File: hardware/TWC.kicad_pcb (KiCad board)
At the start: 2 copper layers, 40 x 75 mm, 46 parts, among them J1 Screw_Terminal_01x04, J2 Conn_02x05_Odd_Even, J3 Conn_02x05_Odd_Even, J4 Conn_01x10_Male, J6 Screw_Terminal_01x02, SW1 SW_Push, SW2 SW_Push, U1 MAX3485, U2 Si7021-A20, U3 TPS56339DDC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

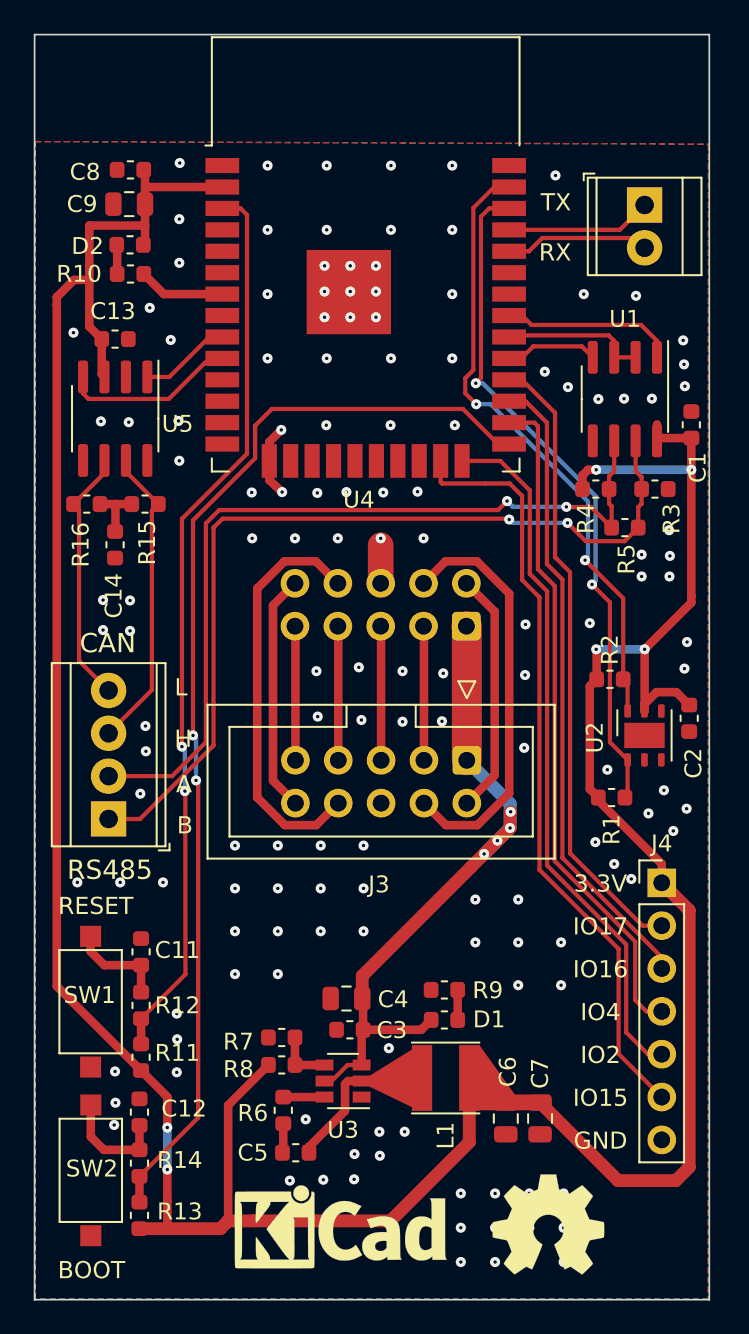
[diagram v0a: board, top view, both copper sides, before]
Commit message: Many small updates, including changing the Buck Converter and temperature sensor to more available parts, changed the screw terminals to the final footprint (0.1" pitch)
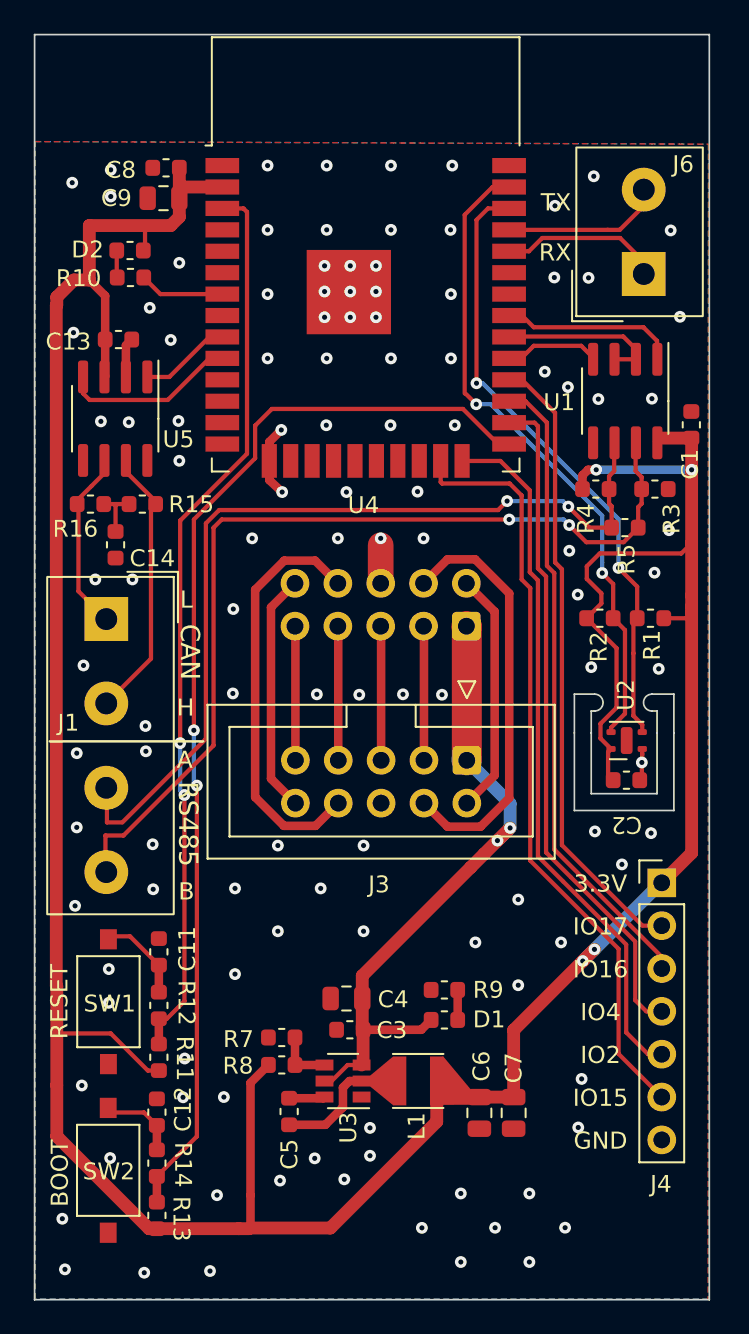
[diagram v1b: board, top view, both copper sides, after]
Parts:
- removed R6: 30, Capacitor_SMD:C_0603_1608Metric
- removed REF**: KiCad-Logo_5mm_SilkScreen, Symbol:KiCad-Logo_5mm_SilkScreen
- removed REF**: OSHW-Symbol_6.7x6mm_SilkScreen, Symbol:OSHW-Symbol_6.7x6mm_SilkScreen
- J1: footprint TerminalBlock_TE-Connectivity:TerminalBlock_TE_282834-4_1x04_P2.54mm_Horizontal -> TerminalBlock_Altech:Altech_AK500_1x04_P5.00
- J6: footprint TerminalBlock_TE-Connectivity:TerminalBlock_TE_282834-2_1x02_P2.54mm_Horizontal -> TerminalBlock_Altech:Altech_AK500_1x02_P5.00
- L1: value 4.7uH -> 3.3uH; footprint Inductor_SMD:L_Taiyo-Yuden_NR-40xx -> Inductor_SMD:L_Taiyo-Yuden_NR-30xx
- R1, R10, R11, R12, R13, R14, R2, R7, R9: footprint Capacitor_SMD:C_0603_1608Metric -> Resistor_SMD:R_0603_1608Metric
- R8: value 31.6 -> 33.2k; footprint Capacitor_SMD:C_0603_1608Metric -> Resistor_SMD:R_0603_1608Metric
- SW1, SW2: footprint Button_Switch_SMD:SW_SPST_CK_PTS636_SX25_XMTR_LFS -> Button_Switch_SMD:SW_SPST_TS_1101_X_X
- U1: value MAX3485 -> SN65HVD11DR
- U2: value Si7021-A20 -> SHTC3; footprint Package_DFN_QFN:DFN-6-1EP_3x3mm_P1mm_EP1.5x2.4mm -> Sensor_Humidity:Sensirion_DFN-4-1EP_2x2mm_P1mm_EP0.7x1.6mm
- U3: value TPS56339DDC -> TPS562201DDCR
- moved J1 11.9 mm to (64.2, 59.6), turned to -90 degrees
- moved R1 10.7 mm to (93.5, 59.6)
- moved C2 5.22 mm to (95.1, 69.2), turned to 0 degrees
- moved R2 4.35 mm to (96.5, 59.6), turned to 180 degrees
- moved J6 4.09 mm to (96.1, 39.2), turned to 90 degrees
- moved C5 2.48 mm to (75.1, 88.8), turned to -90 degrees
- moved C8 2.11 mm to (67.8, 32.9)
- moved C9 2.06 mm to (67.6, 34.7)
- moved L1 1.64 mm to (82.7, 87.0)
- moved C6 1.60 mm to (86.4, 88.9)
- moved C7 1.60 mm to (88.4, 88.9)
- moved U2 1.10 mm to (95.1, 66.8), turned to 180 degrees
- moved SW1 1.05 mm to (64.4, 82.3)
- moved C11 1.05 mm to (67.4, 79.4)
- moved R11 1.05 mm to (67.4, 85.6)
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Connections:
- C5 pad 1: Net-(C5-Pad1) -> /VBST
- J1 pad 1: /B -> /CANL
- J1 pad 2: /A -> /CANH
- J1 pad 3: /CANH -> /A
- J1 pad 4: /CANL -> /B
- J6 pad 1: /TX -> /RX
- J6 pad 2: /RX -> /TX
- U2 pad 1: /SDA -> GND
- U2 pad 2: GND -> /SCL
- U2 pad 3: Net-(U2-Pad3) -> /SDA
- U2 pad 4: Net-(U2-Pad4) -> +3V3
- U2 pad 5: +3V3 -> Net-(U2-Pad5)
- U3 pad 6: Net-(R6-Pad1) -> /VBST
- U4 pad 36: /SDA -> /SCL
- U4 pad 37: /SCL -> /SDA
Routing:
- net GND: track 6.57 -> 11.1 mm, vias 144 -> 118
- net /A: track 50.2 -> 54.5 mm
- net /B: track 52.6 -> 55.4 mm
- net Net-(R6-Pad1): track 2.44 -> 0.00 mm
- net /CANL: track 15.3 -> 12.9 mm
- net /VBST: track 0.00 -> 2.13 mm
- net /SDA: track 40.6 -> 38.7 mm
- net VCC: track 40.8 -> 39.0 mm, vias 4 -> 2
- net /CANH: track 18.2 -> 16.4 mm
- net Net-(C5-Pad1): track 1.75 -> 0.00 mm
- net +3V3: track 202.2 -> 203.7 mm, vias 6 -> 4
- net Net-(C12-Pad2): track 6.67 -> 5.20 mm
- net Net-(C5-Pad2): track 9.42 -> 8.31 mm
- net /RX: track 8.60 -> 9.62 mm
- net /RE: track 8.65 -> 9.59 mm
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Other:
- outline, holes or cut-outs redrawn
- board text added: "Rev 00B 20200727"
- board text removed: "Rev 00A 20200726"

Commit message: Revision 00B with added logos, small cosmetic fixes
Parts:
- added REF**: OSHW-Symbol_6.7x6mm_SilkScreen, Symbol:OSHW-Symbol_6.7x6mm_SilkScreen, F.Cu at (91.6, 95.2)
- added REF**: KiCad-Logo_5mm_SilkScreen, Symbol:KiCad-Logo_5mm_SilkScreen, F.Cu at (79.3, 95.9)
